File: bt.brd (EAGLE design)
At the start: 21.3 x 19.7 mm, 16 parts, among them IC1 BLUETOOTH-RN42 HID, Q1 MOSFET-NCHANNELSMD, Q2 MOSFET-NCHANNELSMD

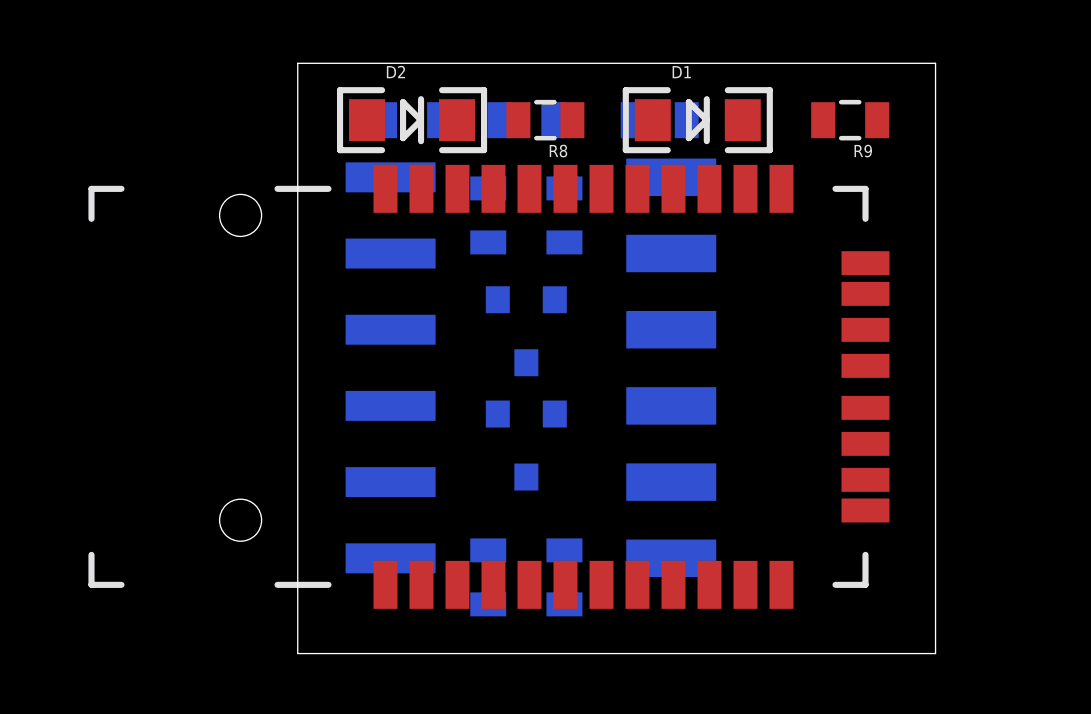
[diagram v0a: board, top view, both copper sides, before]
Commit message: Updated headers to remove annoying holes and now using my own library
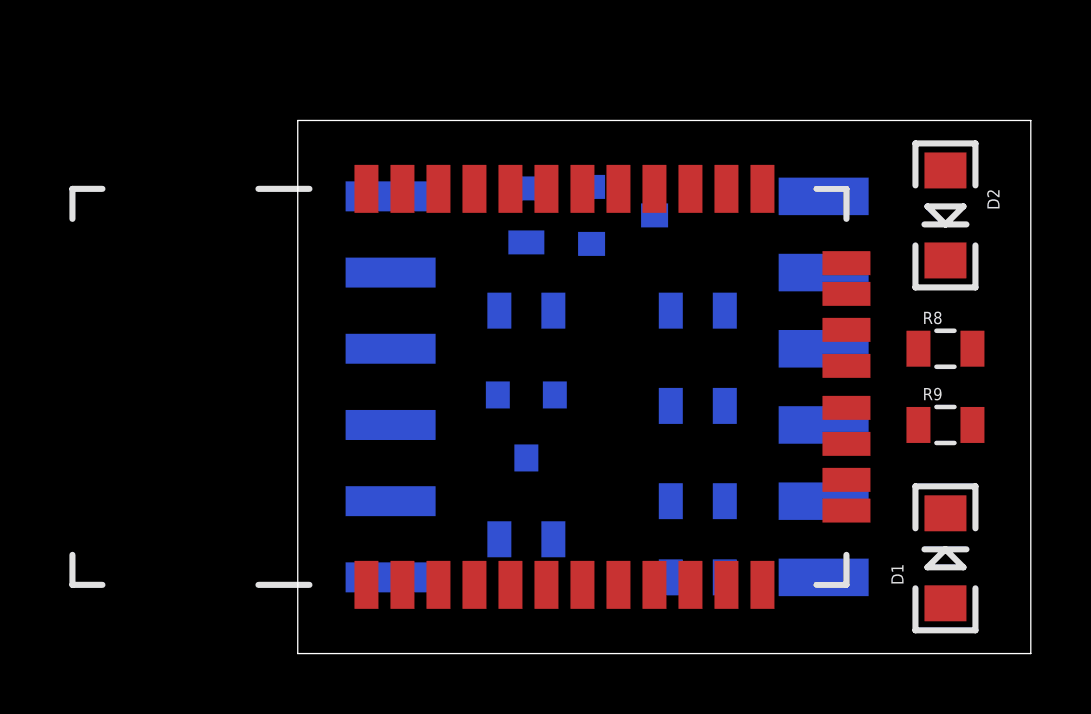
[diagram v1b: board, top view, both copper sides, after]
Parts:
- JP1: device SparkFun-Connectors:1X06-SMD-FEMALE-V2 -> mine:1X06-SMD-FEMALE-V2-NOSILK
- JP2: device SparkFun-Connectors:1X06-SMD -> mine:1X06-SMD-NOHOLES
- moved D2 18.1 mm to (29.8, 14.6), turned to 270 degrees
- moved R2 18.0 mm to (21.6, 2.54), turned to 180 degrees
- moved D1 16.8 mm to (29.8, 3.17), turned to 90 degrees
- moved R8 15.4 mm to (29.8, 10.2), turned to 0 degrees
- moved R7 12.8 mm to (21.6, 5.08), turned to 0 degrees
- moved R1 11.1 mm to (21.6, 8.26), turned to 180 degrees
- moved R9 10.6 mm to (29.8, 7.62), turned to 0 degrees
- moved R3 8.98 mm to (15.9, 11.4), turned to 0 degrees
- moved R6 5.46 mm to (21.6, 11.4), turned to 180 degrees
- moved JP1 5.12 mm to (29.2, 8.89)
- moved Q2 4.96 mm to (19.1, 14.6), turned to 90 degrees
- moved R4 1.80 mm to (15.9, 3.81), turned to 180 degrees
- moved R5 1.27 mm to (15.9, 14.6)
- moved IC1 0.64 mm to (17.1, 8.89)
- moved JP2 0.63 mm to (6.35, 8.89)
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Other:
- board size 21.3 x 19.7 mm -> 24.4 x 17.8 mm

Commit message: Flipped the board around
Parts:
- removed IC1: BLUETOOTH-RN42 HID, SparkFun-RF:RN41
- removed JP1: (no value), mine:1X06-SMD-FEMALE-V2-NOSILK
- removed JP2: RA 6Pin SMD, mine:1X06-SMD-NOHOLES
- added RN-42HID: BLUETOOTH-RN42-NOSILK", mine:RN41
- added UART: RA 6Pin SMD, mine:1X06-SMD-NOHOLES
- added USB: (no value), mine:1X06-SMD-FEMALE-V2-NOSILK
- moved D1 29.0 mm to (3.17, 14.6), turned to 270 degrees
- moved D2 29.0 mm to (3.17, 3.17), turned to 90 degrees
- moved R8 26.8 mm to (3.17, 7.62), turned to 180 degrees
- moved R9 26.8 mm to (3.17, 10.2), turned to 180 degrees
- moved R2 16.3 mm to (11.4, 15.2), turned to 0 degrees
- moved Q2 13.7 mm to (11.4, 3.17), turned to 270 degrees
- moved R7 12.7 mm to (11.4, 12.7), turned to 180 degrees
- moved R5 11.5 mm to (17.1, 3.17), turned to 90 degrees
- moved R6 11.4 mm to (11.4, 6.35), turned to 0 degrees
- moved R1 10.2 mm to (11.4, 9.53), turned to 0 degrees
- moved R4 10.2 mm to (17.1, 14.0), turned to 0 degrees
- moved R3 5.24 mm to (17.1, 6.35), turned to 180 degrees
- moved Q1 2.84 mm to (17.1, 10.2), turned to 0 degrees
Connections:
- net 3.3V: now also USB.6; no longer JP1.6
- net GND: now also RN-42HID.1, RN-42HID.12, RN-42HID.28, RN-42HID.29, UART.1, USB.1; no longer IC1.1, IC1.12, IC1.28, IC1.29, JP1.1, JP2.1
- net N$10: now also RN-42HID.21; no longer IC1.21
- net N$8: now also RN-42HID.19; no longer IC1.19
- net N$9: now also RN-42HID.22; no longer IC1.22
- net UART_CTS: now also RN-42HID.16; no longer IC1.16
- net UART_CTS_5V: now also UART.5; no longer JP2.5
- net UART_RTS: now also RN-42HID.15; no longer IC1.15
- net UART_RTS_5V: now also UART.2; no longer JP2.2
- net UART_RX: now also RN-42HID.13; no longer IC1.13
- net UART_RX_5V: now also UART.3; no longer JP2.3
- net UART_TX: now also RN-42HID.14; no longer IC1.14
- net UART_TX_5V: now also UART.4; no longer JP2.4
- net USB_D+: now also RN-42HID.17, USB.4; no longer IC1.17, JP1.4
- net USB_D-: now also RN-42HID.18, USB.3; no longer IC1.18, JP1.3
- net VCC: now also RN-42HID.11, UART.6, USB.5; no longer IC1.11, JP1.5, JP2.6

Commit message: Changing which pins are the USB data pins to match the standard
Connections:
- net USB_D+: now also RN-42HID.18, USB.3; no longer RN-42HID.17, USB.4
- net USB_D-: now also RN-42HID.17, USB.4; no longer RN-42HID.18, USB.3
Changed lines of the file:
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@@
 <wire x1="12.875" y1="2.29" x2="12.33" y2="15.24" width="0" layer="19" extent="1-16"/>
 </signal>
-<signal name="USB_D-">
+<signal name="USB_D+">
 <contactref element="USB" pad="3"/>
 <contactref element="RN-42HID" pad="18"/>
 <wire x1="15.275" y1="2.29" x2="7.235" y2="10.16" width="0" layer="19" extent="1-16"/>
 </signal>
-<signal name="USB_D+">
+<signal name="USB_D-">
 <contactref element="USB" pad="4"/>
 <contactref element="RN-42HID" pad="17"/>
